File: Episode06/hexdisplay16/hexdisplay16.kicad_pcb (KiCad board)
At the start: 2 copper layers, 24 parts, among them J1 Conn_02x05_Counter_Clockwise, J2 Conn_02x05_Counter_Clockwise, J3 Conn_02x05_Counter_Clockwise, J4 Conn_02x05_Counter_Clockwise, J5 Conn_01x02, J6 Conn_01x16, J7 Conn_01x06, Q1 MMBT3906, Q2 MMBT3906, Q3 MMBT3906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

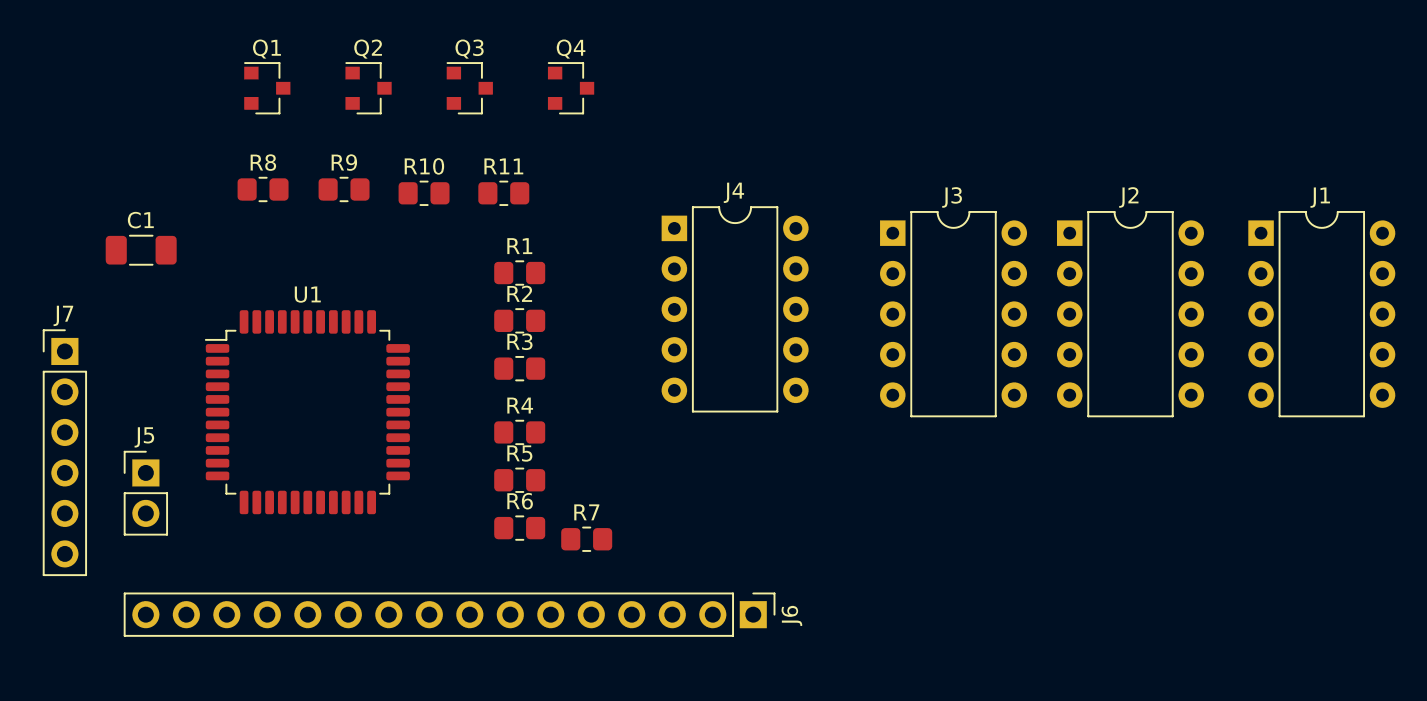
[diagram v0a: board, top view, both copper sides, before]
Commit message: component placement is reasonable?
Now need to do routing.
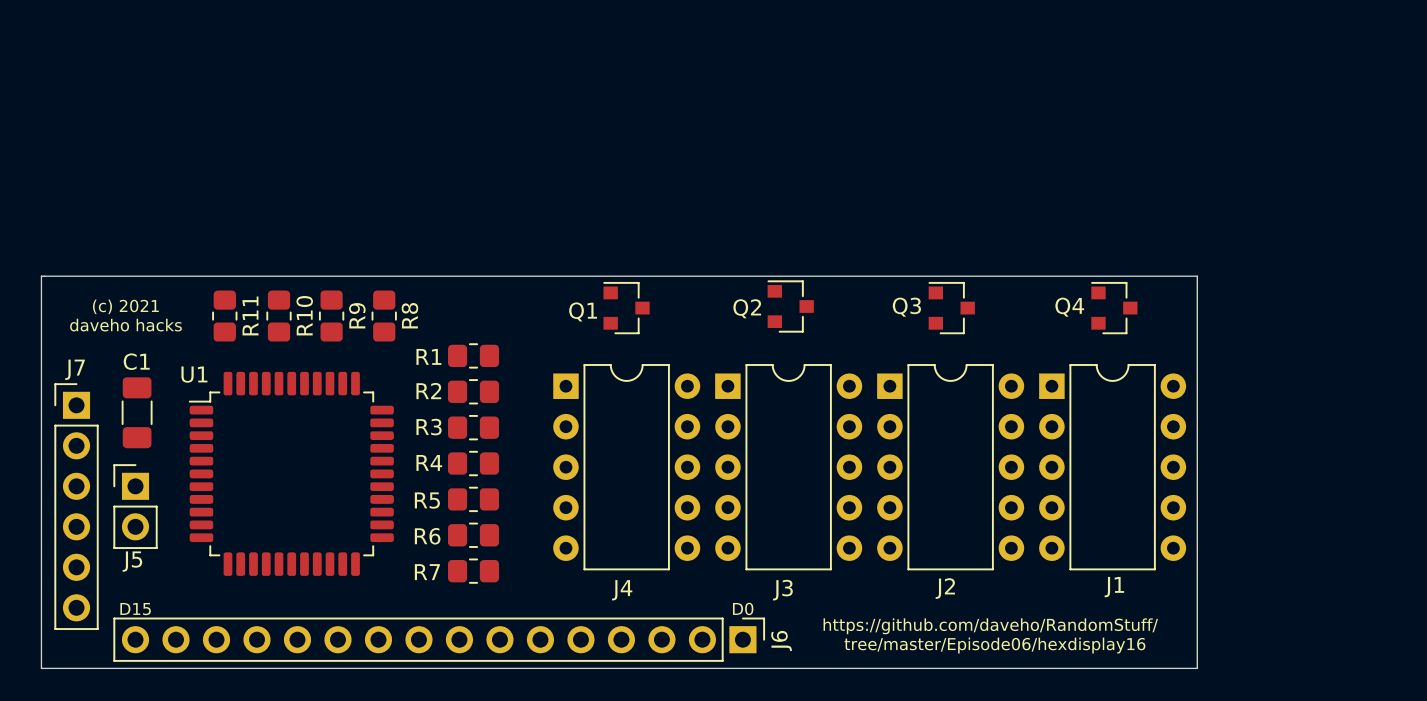
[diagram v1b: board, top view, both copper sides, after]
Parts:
- moved Q4 36.8 mm to (143.3, 119.2)
- moved Q3 33.2 mm to (133.1, 119.2)
- moved Q2 29.8 mm to (123.0, 119.1)
- moved Q1 26.4 mm to (112.7, 119.2)
- moved R11 19.1 mm to (87.5, 119.7), turned to 270 degrees
- moved J1 16.3 mm to (139.4, 124.1)
- moved J2 14.8 mm to (129.2, 124.1)
- moved J3 14.1 mm to (119.1, 124.1)
- moved J4 12.0 mm to (108.9, 124.1)
- moved R10 11.9 mm to (90.9, 119.7), turned to 270 degrees
- moved R8 11.0 mm to (97.5, 119.7), turned to 270 degrees
- moved C1 10.2 mm to (82.0, 125.8), turned to 90 degrees
- moved R9 7.98 mm to (94.2, 119.7), turned to 270 degrees
- moved R7 7.38 mm to (103.1, 135.7)
- moved R1 5.95 mm to (103.1, 122.2)
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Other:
- board outline added: 72.5 x 24.6 mm
- board text added: "(c) 2021 daveho hacks"
- board text added: "D0"
- board text added: "D15"
- board text added: "https://github.com/daveho/RandomStuff/ tree/master/Episode06/hexdisplay16"

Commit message: started the signal routing
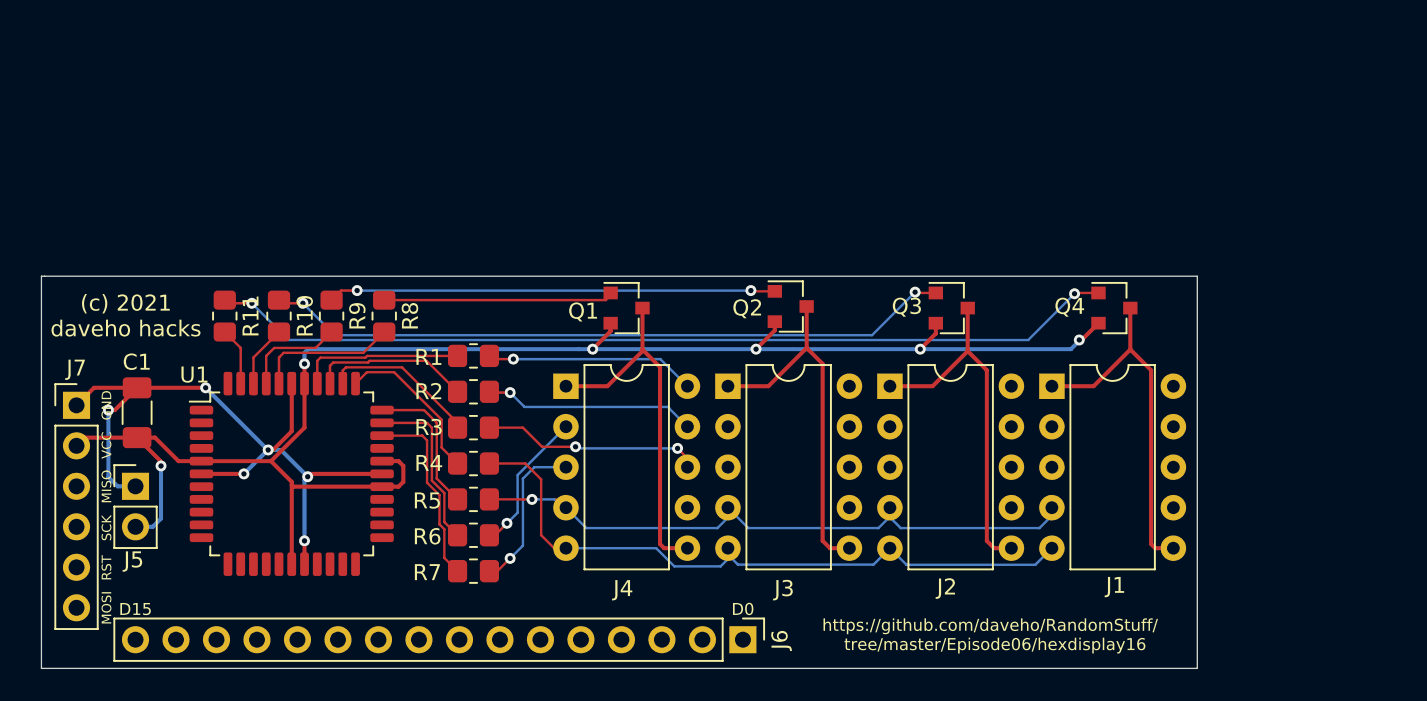
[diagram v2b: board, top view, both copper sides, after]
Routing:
- net VCC: track 0.00 -> 102.1 mm, vias 0 -> 6
- net Net-(Q4-Pad1): track 0.00 -> 57.1 mm, vias 0 -> 2
- net GND: track 0.00 -> 45.8 mm, vias 0 -> 6
- net Net-(Q3-Pad1): track 0.00 -> 43.3 mm, vias 0 -> 2
- net /D: track 0.00 -> 42.8 mm
- net /E: track 0.00 -> 41.5 mm, vias 0 -> 1
- net Net-(Q2-Pad1): track 0.00 -> 28.1 mm, vias 0 -> 2
- net /CA2: track 0.00 -> 22.9 mm
- net /CA1: track 0.00 -> 22.9 mm
- net /CA4: track 0.00 -> 22.7 mm
- net /CA3: track 0.00 -> 22.6 mm
- net Net-(Q1-Pad1): track 0.00 -> 14.7 mm
- net /C: track 0.00 -> 13.8 mm, vias 0 -> 2
- net /B: track 0.00 -> 13.3 mm, vias 0 -> 1
- net /A: track 0.00 -> 13.2 mm, vias 0 -> 1
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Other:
- net class Default: clearance 0.2 -> 0.1524; trace_width 0.25 -> 0.1524; via_dia 0.8 -> 0.6858; via_drill 0.4 -> 0.3302
- rule pad_to_mask_clearance: 0 -> 0.0508
- rule trace_clearance: 0.2 -> 0.1524
- rule trace_min: 0.2 -> 0.1524
- rule via_min_drill: 0.3 -> 0.3302
- rule via_min_size: 0.4 -> 0.6858
- board text added: "GND"
- board text added: "MISO"
- board text added: "MOSI"
- board text added: "RST"
- board text added: "SCK"
- board text added: "VCC"

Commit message: finishing routing signals
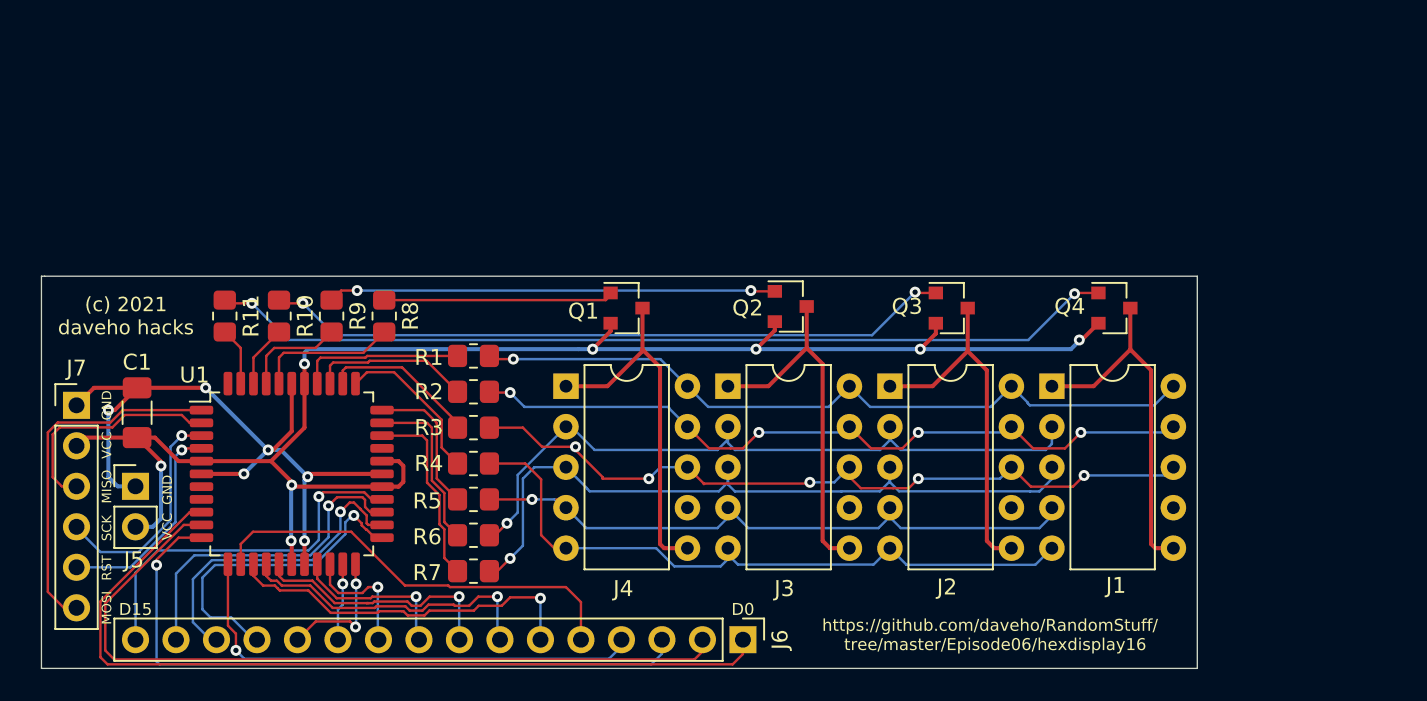
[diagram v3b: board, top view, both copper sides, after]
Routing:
- net /D0: track 0.00 -> 53.8 mm
- net /D1: track 0.00 -> 49.7 mm
- net /D2: track 0.00 -> 42.7 mm, vias 0 -> 1
- net /G: track 9.96 -> 46.9 mm
- net /F: track 9.00 -> 45.8 mm
- net /C: track 13.8 -> 49.0 mm, vias 2 -> 5
- net /B: track 13.3 -> 47.2 mm, vias 1 -> 4
- net /A: track 13.2 -> 46.9 mm
- net /D3: track 0.00 -> 30.8 mm, vias 0 -> 1
- net /D4: track 0.00 -> 27.1 mm
- net /D15: track 0.00 -> 23.5 mm, vias 0 -> 1
- net /D5: track 0.00 -> 22.9 mm, vias 0 -> 1
- net /MOSI: track 0.00 -> 22.4 mm
- net /D14: track 0.00 -> 20.9 mm, vias 0 -> 1
- net /D12: track 0.00 -> 20.2 mm, vias 0 -> 1
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
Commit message: added ground planes
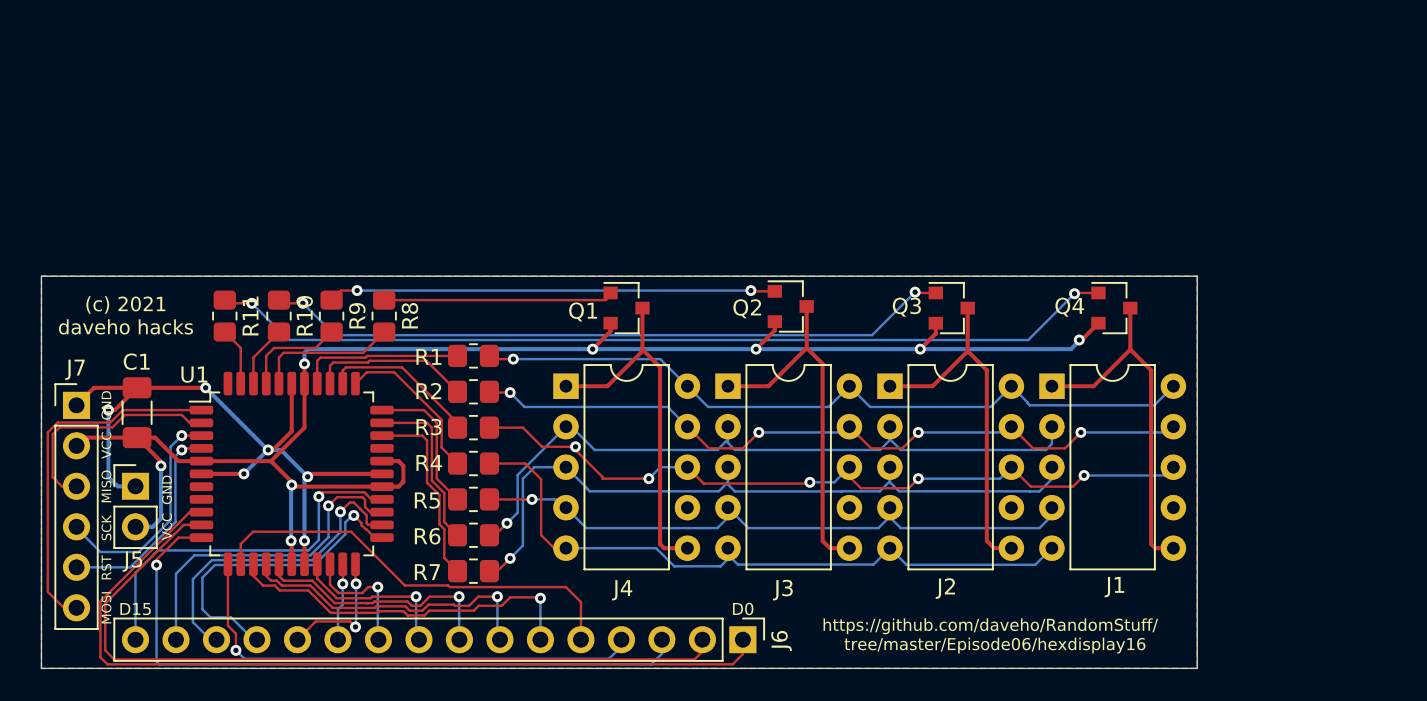
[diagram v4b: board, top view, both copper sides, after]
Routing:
- added copper zone on B.Cu, net GND
- added copper zone on F.Cu, net GND
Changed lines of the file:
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@@
   (segment (start 88.5 121.7) (end 87.5 120.7) (width 0.1524) (layer F.Cu) (net 52))
   (segment (start 88.5 123.9375) (end 88.5 121.7) (width 0.1524) (layer F.Cu) (net 52))
+  (zone (net 2) (net_name GND) (layer F.Cu) (hatch edge 0.508)
+    (connect_pads (clearance 0.508))
+    (min_thickness 0.254)
+    (fill yes (arc_segments 32) (thermal_gap 0.508) (thermal_bridge_width 0.508))
+    (polygon
+      (pts
+        (xy 148.5 141.8) (xy 76 141.8) (xy 76 117.2) (xy 148.5 117.2)
+      )
+    )
+  )
+  (zone (net 2) (net_name GND) (layer B.Cu) (hatch edge 0.508)
+    (connect_pads (clearance 0.508))
+    (min_thickness 0.254)
+    (fill yes (arc_segments 32) (thermal_gap 0.508) (thermal_bridge_width 0.508))
+    (polygon
+      (pts
+        (xy 148.5 141.8) (xy 76 141.8) (xy 76 117.2) (xy 148.5 117.2)
+      )
+    )
+  )
 )
